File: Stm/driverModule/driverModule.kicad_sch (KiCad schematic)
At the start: 4 parts

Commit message: routing
Finished PCB routing
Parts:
- added TP4, TP5, TP6, TP7: TestPoint_Small, TestPoint:TestPoint_Pad_1.0x1.0mm, symbol Connector:TestPoint_Small
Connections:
- net MirrorSpiChipSelect: now also TP4.1
- net SpiClock: now also TP5.1
- net SpiMasterInput: now also TP6.1
- net SpiMasterOutput: now also TP7.1
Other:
- sheet CPU Board Connector ports: added +5V; removed none

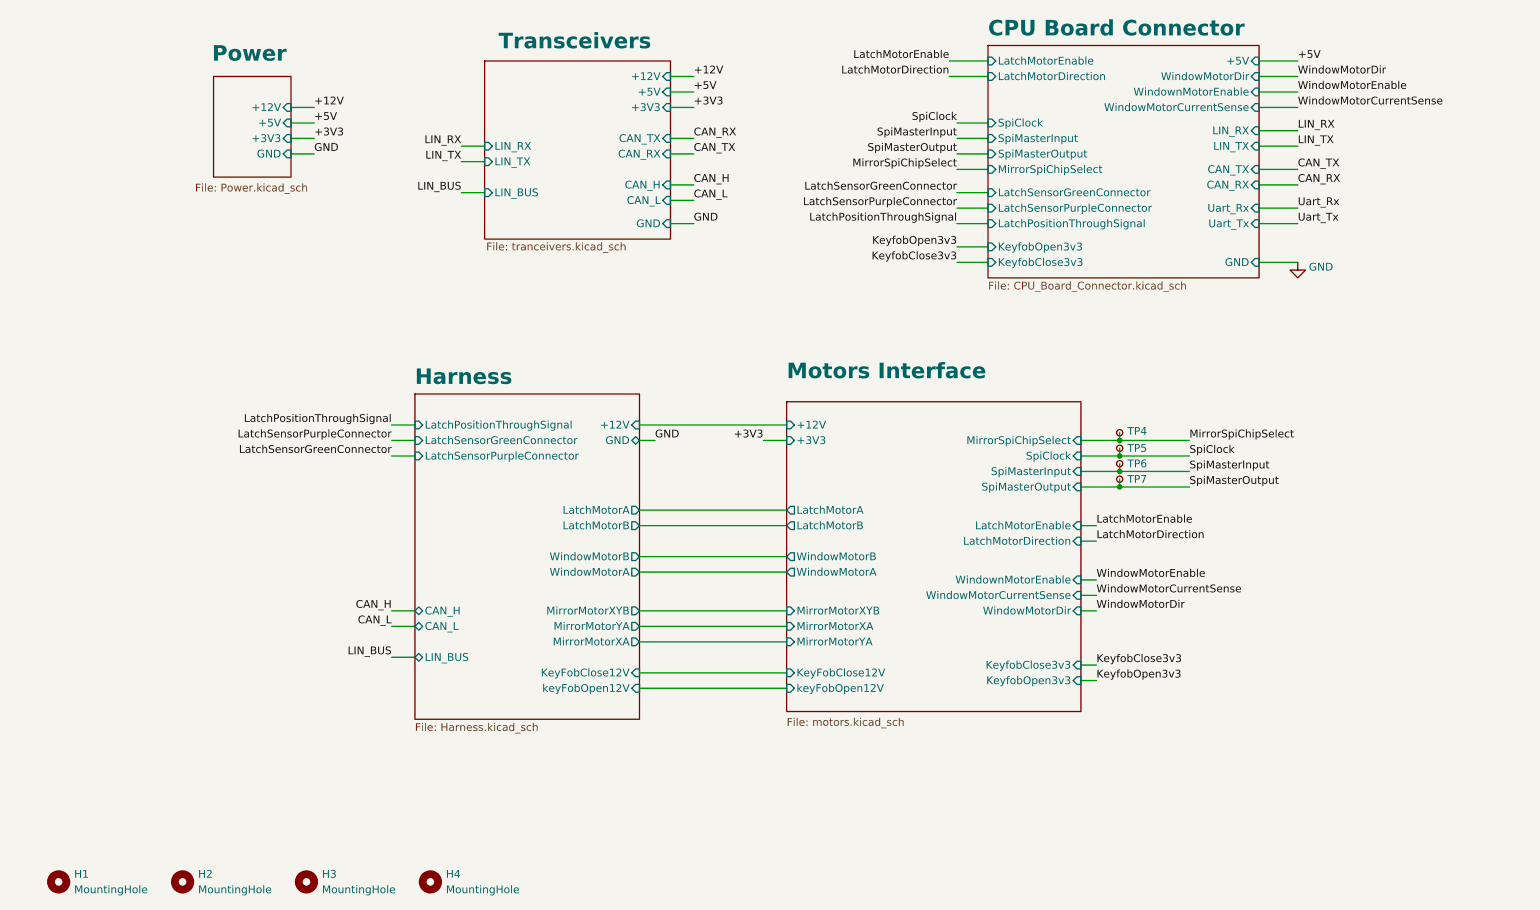
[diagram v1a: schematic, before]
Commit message: ADC
Added adc to read passenger input signals
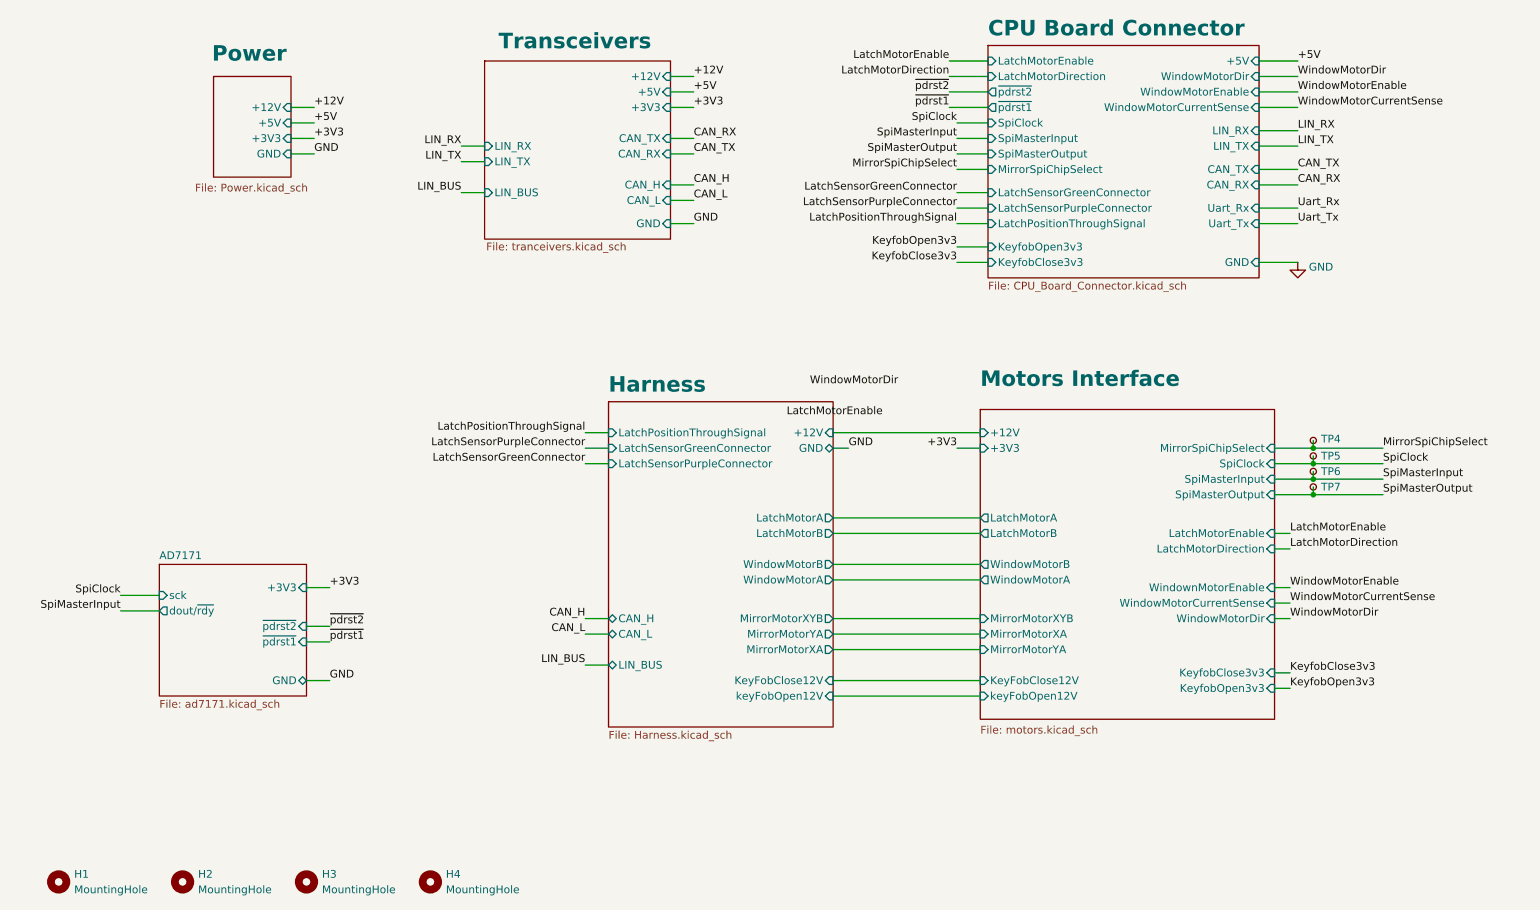
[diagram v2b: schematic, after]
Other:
- added sheet AD7171 (ad7171.kicad_sch)
- sheet CPU Board Connector ports: added WindowMotorEnable, ~{pdrst1}, ~{pdrst2}; removed WindownMotorEnable
- moved on the sheet: TP4, TP5, TP6, TP7
